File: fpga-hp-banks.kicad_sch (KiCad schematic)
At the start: 9 parts, among them U34 XCAU25P-2FFVB676I

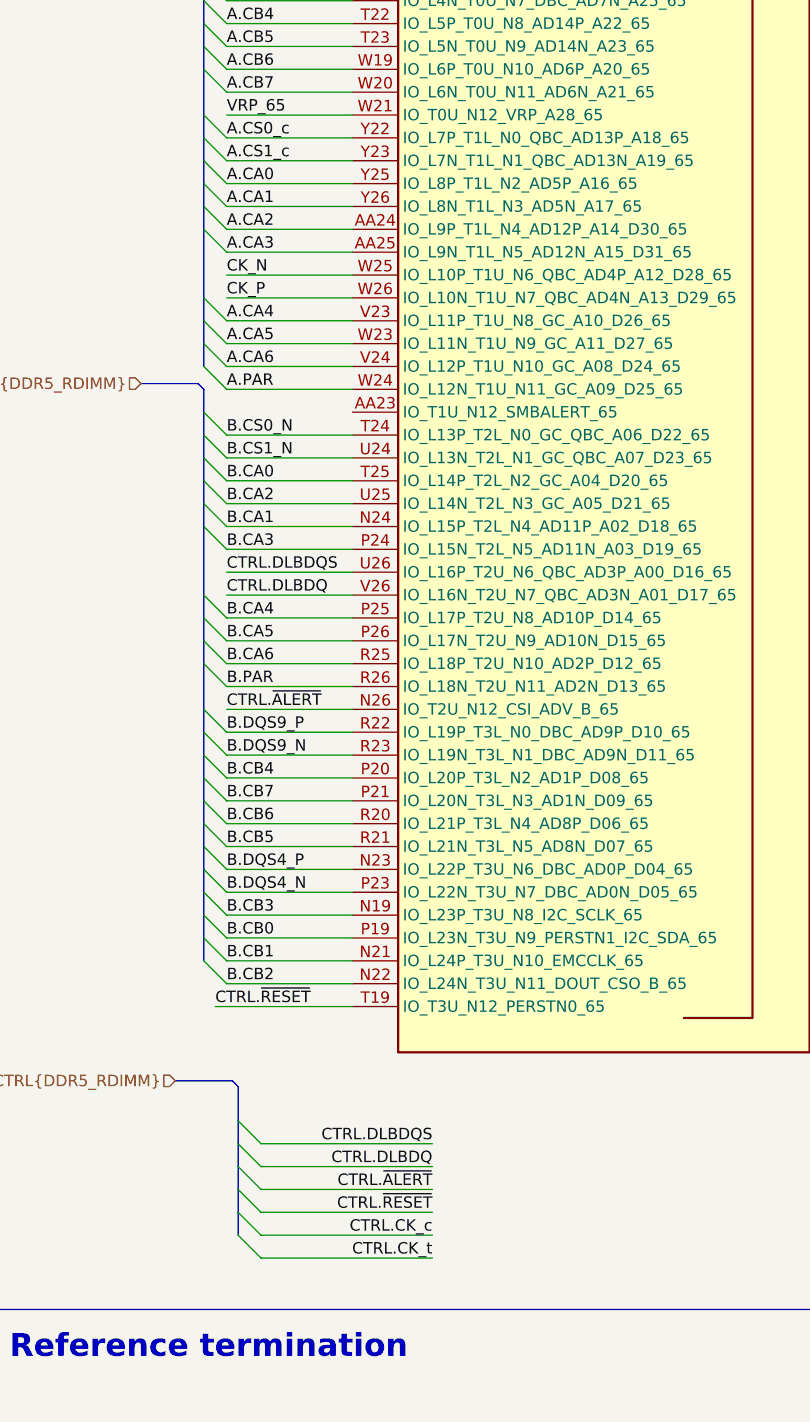
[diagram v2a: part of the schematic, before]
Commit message: [#66521] Add Layout for A.CA[0..7], B.CA[0..7]
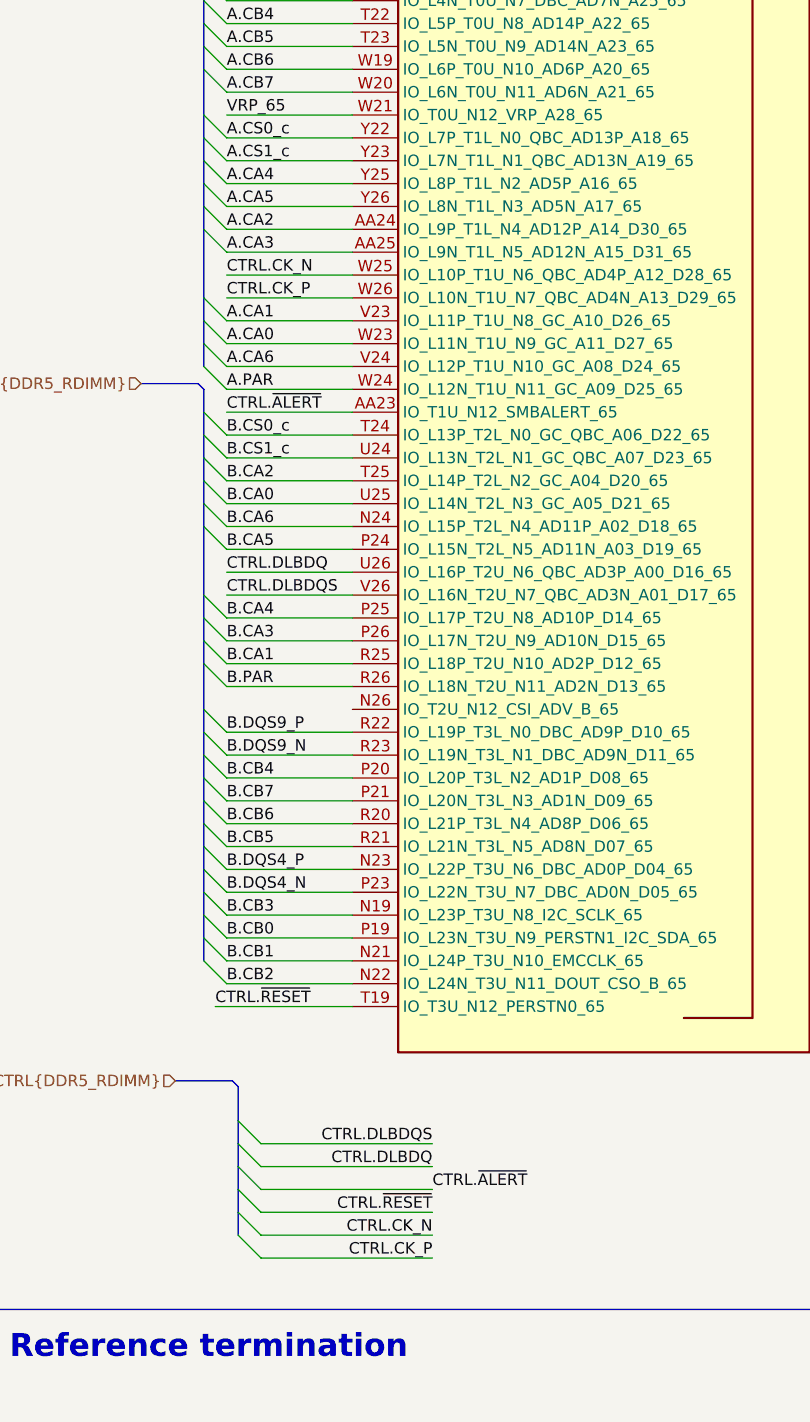
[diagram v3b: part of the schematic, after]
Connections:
- net A.CA0: now also U34.W23 (IO_L11N_T1U_N9_GC_A11_D27_65); no longer U34.Y25 (IO_L8P_T1L_N2_AD5P_A16_65)
- net A.CA1: now also U34.V23 (IO_L11P_T1U_N8_GC_A10_D26_65); no longer U34.Y26 (IO_L8N_T1L_N3_AD5N_A17_65)
- net A.CA4: now also U34.Y25 (IO_L8P_T1L_N2_AD5P_A16_65); no longer U34.V23 (IO_L11P_T1U_N8_GC_A10_D26_65)
- net A.CA5: now also U34.Y26 (IO_L8N_T1L_N3_AD5N_A17_65); no longer U34.W23 (IO_L11N_T1U_N9_GC_A11_D27_65)
- net B.CA0: now also U34.U25 (IO_L14N_T2L_N3_GC_A05_D21_65); no longer U34.T25 (IO_L14P_T2L_N2_GC_A04_D20_65)
- net B.CA1: now also U34.R25 (IO_L18P_T2U_N10_AD2P_D12_65); no longer U34.N24 (IO_L15P_T2L_N4_AD11P_A02_D18_65)
- net B.CA2: now also U34.T25 (IO_L14P_T2L_N2_GC_A04_D20_65); no longer U34.U25 (IO_L14N_T2L_N3_GC_A05_D21_65)
- net B.CA3: now also U34.P26 (IO_L17N_T2U_N9_AD10N_D15_65); no longer U34.P24 (IO_L15N_T2L_N5_AD11N_A03_D19_65)
- net B.CA5: now also U34.P24 (IO_L15N_T2L_N5_AD11N_A03_D19_65); no longer U34.P26 (IO_L17N_T2U_N9_AD10N_D15_65)
- net B.CA6: now also U34.N24 (IO_L15P_T2L_N4_AD11P_A02_D18_65); no longer U34.R25 (IO_L18P_T2U_N10_AD2P_D12_65)
- net CTRL.DLBDQ: now also U34.U26 (IO_L16P_T2U_N6_QBC_AD3P_A00_D16_65); no longer U34.V26 (IO_L16N_T2U_N7_QBC_AD3N_A01_D17_65)
- net CTRL.DLBDQS: now also U34.V26 (IO_L16N_T2U_N7_QBC_AD3N_A01_D17_65); no longer U34.U26 (IO_L16P_T2U_N6_QBC_AD3P_A00_D16_65)
- net CTRL.~{ALERT}: now also U34.AA23 (IO_T1U_N12_SMBALERT_65); no longer U34.N26 (IO_T2U_N12_CSI_ADV_B_65)
- net B.CS0_N renamed B.CS0_c
- net B.CS1_N renamed B.CS1_c
- net CK_N renamed CTRL.CK_N
- net CK_P renamed CTRL.CK_P
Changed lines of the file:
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@@
     (stroke (width 0) (type default))
   )
-  (wire (pts (xy 135.89 154.94) (xy 149.86 154.94))
+  (wire (pts (xy 135.89 121.92) (xy 149.86 121.92))
     (stroke (width 0) (type default))
   )
@@
     (effects (font (size 1.27 1.27)) (justify left bottom))
   )
-  (label "A.CA4" (at 135.89 111.76 0) (fields_autoplaced)
+  (label "A.CA4" (at 135.89 96.52 0) (fields_autoplaced)
     (effects (font (size 1.27 1.27)) (justify left bottom))
   )
@@
     (effects (font (size 1.27 1.27)) (justify left bottom))
   )
-  (label "B.CA6" (at 135.89 149.86 0) (fields_autoplaced)
+  (label "B.CA6" (at 135.89 134.62 0) (fields_autoplaced)
     (effects (font (size 1.27 1.27)) (justify left bottom))
   )
@@
     (effects (font (size 1.27 1.27)) (justify left bottom))
   )
-  (label "CTRL.~{ALERT}" (at 135.89 154.94 0) (fields_autoplaced)
+  (label "CTRL.~{ALERT}" (at 135.89 121.92 0) (fields_autoplaced)
     (effects (font (size 1.27 1.27)) (justify left bottom))
   )
@@
     (effects (font (size 1.27 1.27)) (justify left bottom))
   )
-  (label "A.CA5" (at 135.89 114.3 0) (fields_autoplaced)
+  (label "A.CA5" (at 135.89 99.06 0) (fields_autoplaced)
     (effects (font (size 1.27 1.27)) (justify left bottom))
   )
@@
     (effects (font (size 1.27 1.27)) (justify left bottom))
   )
-  (label "CTRL.CK_c" (at 158.75 213.36 180) (fields_autoplaced)
+  (label "CTRL.CK_N" (at 158.75 213.36 180) (fields_autoplaced)
     (effects (font (size 1.27 1.27)) (justify right bottom))
   )
@@
     (effects (font (size 1.27 1.27)) (justify left bottom))
   )
-  (label "B.CA1" (at 135.89 134.62 0) (fields_autoplaced)
-    (effects (font (size 1.27 1.27)) (justify left bottom))
-  )
-  (label "B.CA3" (at 135.89 137.16 0) (fields_autoplaced)
+  (label "B.CA1" (at 135.89 149.86 0) (fields_autoplaced)
+    (effects (font (size 1.27 1.27)) (justify left bottom))
+  )
+  (label "B.CA3" (at 135.89 147.32 0) (fields_autoplaced)
     (effects (font (size 1.27 1.27)) (justify left bottom))
   )
@@
     (effects (font (size 1.27 1.27)) (justify left bottom))
   )
-  (label "CTRL.~{ALERT}" (at 158.75 208.28 180) (fields_autoplaced)
-    (effects (font (size 1.27 1.27)) (justify right bottom))
+  (label "CTRL.~{ALERT}" (at 158.75 208.28 0) (fields_autoplaced)
+    (effects (font (size 1.27 1.27)) (justify left bottom))
   )
   (label "B.DQ6" (at 245.11 86.36 0) (fields_autoplaced)
@@
     (effects (font (size 1.27 1.27)) (justify left bottom))
   )
+  (label "CTRL.CK_P" (at 135.89 109.22 0) (fields_autoplaced)
+    (effects (font (size 1.27 1.27)) (justify left bottom))
+  )
   (label "VRP_67" (at 419.1 -138.43 0) (fields_autoplaced)
     (effects (font (size 1.27 1.27)) (justify left bottom))
@@
     (effects (font (size 1.27 1.27)) (justify left bottom))
   )
-  (label "B.CA2" (at 135.89 132.08 0) (fields_autoplaced)
-    (effects (font (size 1.27 1.27)) (justify left bottom))
-  )
-  (label "A.CA0" (at 135.89 96.52 0) (fields_autoplaced)
+  (label "B.CA2" (at 135.89 129.54 0) (fields_autoplaced)
+    (effects (font (size 1.27 1.27)) (justify left bottom))
+  )
+  (label "A.CA0" (at 135.89 114.3 0) (fields_autoplaced)
     (effects (font (size 1.27 1.27)) (justify left bottom))
   )
@@
     (effects (font (size 1.27 1.27)) (justify left bottom))
   )
-  (label "B.CA0" (at 135.89 129.54 0) (fields_autoplaced)
-    (effects (font (size 1.27 1.27)) (justify left bottom))
-  )
-  (label "CTRL.DLBDQS" (at 135.89 139.7 0) (fields_autoplaced)
+  (label "B.CA0" (at 135.89 132.08 0) (fields_autoplaced)
+    (effects (font (size 1.27 1.27)) (justify left bottom))
+  )
+  (label "CTRL.DLBDQS" (at 135.89 142.24 0) (fields_autoplaced)
     (effects (font (size 1.27 1.27)) (justify left bottom))
   )
@@
     (effects (font (size 1.27 1.27)) (justify left bottom))
   )
-  (label "CTRL.DLBDQ" (at 135.89 142.24 0) (fields_autoplaced)
+  (label "CTRL.DLBDQ" (at 135.89 139.7 0) (fields_autoplaced)
     (effects (font (size 1.27 1.27)) (justify left bottom))
   )
@@
     (effects (font (size 1.27 1.27)) (justify left bottom))
   )
-  (label "A.CA1" (at 135.89 99.06 0) (fields_autoplaced)
+  (label "A.CA1" (at 135.89 111.76 0) (fields_autoplaced)
     (effects (font (size 1.27 1.27)) (justify left bottom))
   )
@@
     (effects (font (size 1.27 1.27)) (justify left bottom))
   )
+  (label "CTRL.CK_N" (at 135.89 106.68 0) (fields_autoplaced)
+    (effects (font (size 1.27 1.27)) (justify left bottom))
+  )
   (label "B.DQS7_N" (at 245.11 144.78 0) (fields_autoplaced)
     (effects (font (size 1.27 1.27)) (justify left bottom))
@@
     (effects (font (size 1.27 1.27)) (justify left bottom))
   )
-  (label "B.CA5" (at 135.89 147.32 0) (fields_autoplaced)
+  (label "B.CA5" (at 135.89 137.16 0) (fields_autoplaced)
     (effects (font (size 1.27 1.27)) (justify left bottom))
   )
@@
     (effects (font (size 1.27 1.27)) (justify left bottom))
   )
-  (label "B.CS0_N" (at 135.89 124.46 0) (fields_autoplaced)
-    (effects (font (size 1.27 1.27)) (justify left bottom))
-  )
-  (label "CK_N" (at 135.89 106.68 0) (fields_autoplaced)
+  (label "B.CS0_c" (at 135.89 124.46 0) (fields_autoplaced)
     (effects (font (size 1.27 1.27)) (justify left bottom))
   )
@@
   )
   (label "B.DQS5_N" (at 245.11 78.74 0) (fields_autoplaced)
-    (effects (font (size 1.27 1.27)) (justify left bottom))
-  )
-  (label "CK_P" (at 135.89 109.22 0) (fields_autoplaced)
     (effects (font (size 1.27 1.27)) (justify left bottom))
   )
@@
     (effects (font (size 1.27 1.27)) (justify left bottom))
   )
-  (label "CTRL.CK_t" (at 158.75 215.9 180) (fields_autoplaced)
+  (label "CTRL.CK_P" (at 158.75 215.9 180) (fields_autoplaced)
     (effects (font (size 1.27 1.27)) (justify right bottom))
   )
@@
     (effects (font (size 1.27 1.27)) (justify left bottom))
   )
-  (label "B.CS1_N" (at 135.89 127 0) (fields_autoplaced)
-    (effects (font (size 1.27 1.27)) (justify left bottom))
-  )
+  (label "B.CS1_c" (at 135.89 127 0) (fields_autoplaced)
+    (effects (font (size 1.27 1.27)) (justify left bottom))
+  )
